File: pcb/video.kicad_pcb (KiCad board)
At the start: 4 copper layers, 159.9 x 99.9 mm, 174 parts, among them J1 09031966921, J3 Conn_01x06, J4 Conn_01x06, J5 Conn_01x06, J6 Conn_01x06, J7 DB15_Female_HighDensity, J8 HDMI_A, U1 NCP115, U10 NCA9306DPH, U2 LP3853ESX-3.3/NOPB, U3 LCMXO2-1200HC-4TG100I, U4 LCMXO2-7000HC-4TG144C, U5 THS8136, U6 TFP410PAP, U7 ESD224DQA, U8 ESD224DQA, U9 PCA9540BDP, X1 ASV-xxxMHz

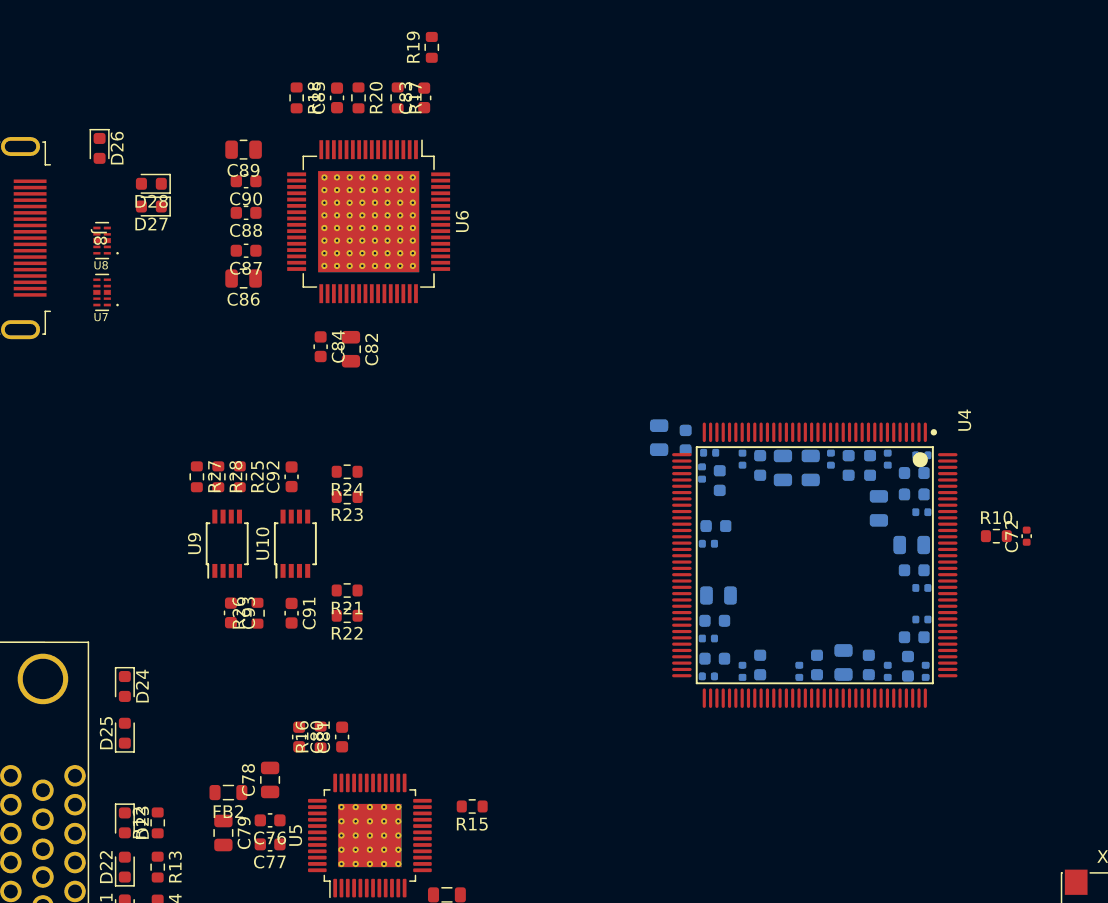
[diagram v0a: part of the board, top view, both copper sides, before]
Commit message: add traces for hdmi interface with proper anti crosstalk
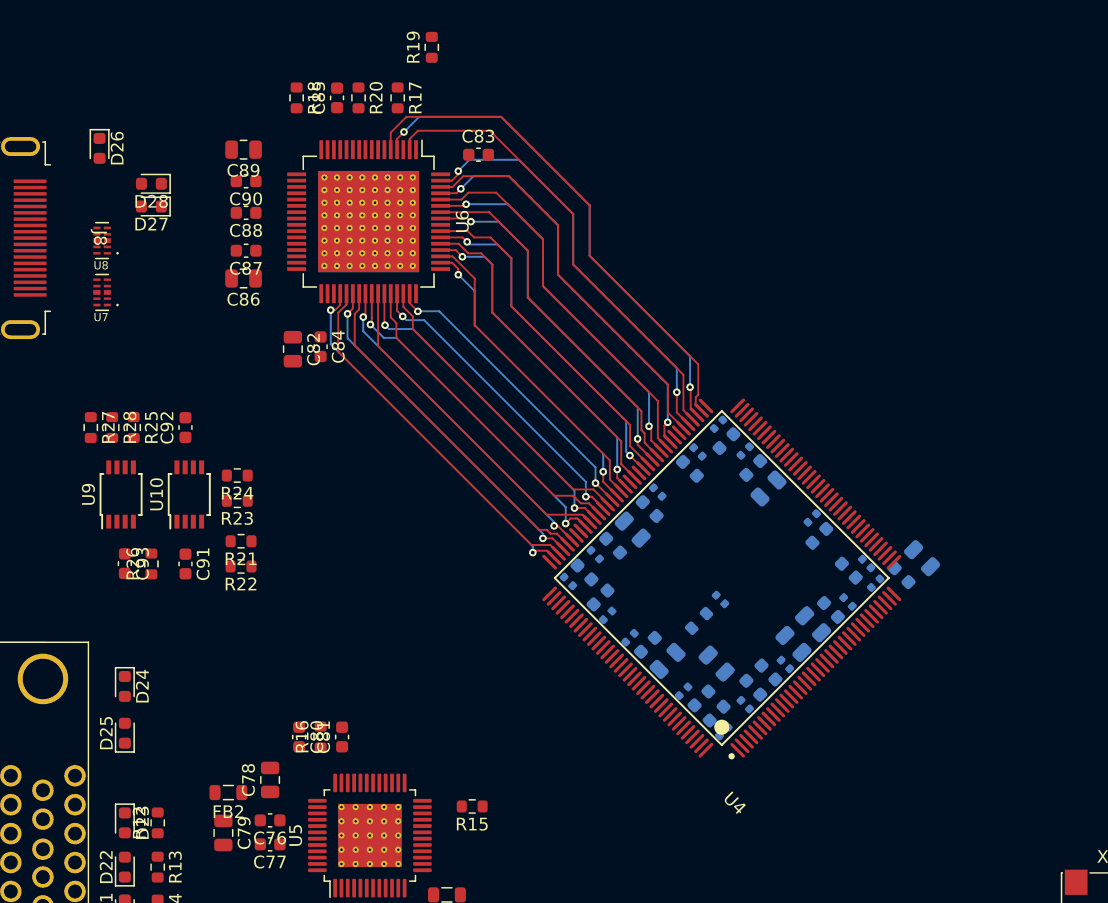
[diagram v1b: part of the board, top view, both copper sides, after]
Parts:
- C72, R10: moved to B.Cu
- moved C39 29.2 mm to (108.0, 96.3), turned to -45 degrees
- moved C38 26.9 mm to (120.3, 108.2), turned to 45 degrees
- moved C35 26.7 mm to (109.3, 95.6), turned to -45 degrees
- moved C47 25.0 mm to (110.5, 97.6), turned to 45 degrees
- moved C49 24.9 mm to (110.1, 94.2), turned to -45 degrees
- moved C42 24.9 mm to (111.1, 99.0), turned to 45 degrees
- moved C72 24.8 mm to (120.0, 97.7), turned to -45 degrees
- moved C36 24.6 mm to (119.7, 106.8), turned to 45 degrees
- moved R10 24.5 mm to (118.3, 99.4), turned to 45 degrees
- moved C44 23.6 mm to (117.1, 105.0), turned to 45 degrees
- moved C43 23.4 mm to (112.9, 100.8), turned to 45 degrees
- moved C46 23.3 mm to (118.5, 105.6), turned to 45 degrees
- moved C33 22.9 mm to (136.0, 94.5), turned to -45 degrees
- moved C71 22.5 mm to (122.0, 106.1), turned to 135 degrees
- moved C53 22.3 mm to (111.5, 93.5), turned to -45 degrees
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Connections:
- net /Video FPGA - Power/PLLIN renamed /Video FPGA/PLLIN
- net /Video FPGA - Power/TCK renamed /Video FPGA/TCK
- net /Video FPGA - Power/TDI renamed /Video FPGA/TDI
- net /Video FPGA - Power/TDO renamed /Video FPGA/TDO
- net /Video FPGA - Power/TMS renamed /Video FPGA/TMS
- D17 pad 2: /Video FPGA - Power/SN -> /Video FPGA/SN
- J6 pad 5: /Video FPGA - Power/SN -> /Video FPGA/SN
- R11 pad 2: /Video FPGA - Power/SN -> /Video FPGA/SN
- U4 pad 100: unconnected-(U4B-PR5A/(DQ0)) -> HDMI_D18
- U4 pad 103: unconnected-(U4B-PR4C) -> HDMI_D19
- U4 pad 104: unconnected-(U4B-PR3B/R_GPLLC_IN/(DQ0)) -> HDMI_D20
- U4 pad 105: unconnected-(U4B-PR3A/R_GPLLT_IN/(DQ0)) -> HDMI_D21
- U4 pad 106: unconnected-(U4B-PR2B/R_GPLLC_FB/(DQ0)) -> HDMI_D22
- U4 pad 107: unconnected-(U4B-PR2A/R_GPLLT_FB/(DQ0)) -> HDMI_D23
- U4 pad 70: /Video FPGA - Power/SN -> unconnected-(U4C-PB38A/SN)
- U4 pad 74: unconnected-(U4B-PR24A/(DQ1)) -> HDMI_VSYNC
- U4 pad 75: unconnected-(U4B-PR23B/(DQ1)) -> HDMI_HSYNC
- U4 pad 76: unconnected-(U4B-PR23A/(DQ1)) -> HDMI_DE
- U4 pad 77: unconnected-(U4B-PR21B/(DQ1)) -> HDMI_D0
- U4 pad 78: unconnected-(U4B-PR21A/(DQ1)) -> HDMI_D1
- U4 pad 81: unconnected-(U4B-PR18B/(DQ1)) -> HDMI_D2
- U4 pad 82: unconnected-(U4B-PR18A/(DQ1)) -> HDMI_D3
- U4 pad 83: unconnected-(U4B-PR17B/(DQ1)) -> HDMI_D4
- U4 pad 84: unconnected-(U4B-PR17A/(DQ1)) -> HDMI_D5
- U4 pad 85: unconnected-(U4B-PR16B/(DQS1N)) -> HDMI_CLK
- U4 pad 86: unconnected-(U4B-PR16A/(DQS1)) -> HDMI_D6
- U4 pad 87: unconnected-(U4B-PR15B) -> HDMI_D7
- U4 pad 89: unconnected-(U4B-PR15A) -> HDMI_D8
- U4 pad 91: unconnected-(U4B-PR12B/PCLKC1_0/(DQ0)) -> HDMI_D9
- U4 pad 92: unconnected-(U4B-PR12A/PCLKT1_0/(DQ0)) -> HDMI_D10
- U4 pad 93: unconnected-(U4B-PR11B/(DQS0N)) -> HDMI_D11
- U4 pad 94: unconnected-(U4B-PR11A/(DQS0)) -> HDMI_D12
- U4 pad 95: unconnected-(U4B-PR9B/(DQ0)) -> HDMI_D13
- U4 pad 96: unconnected-(U4B-PR9A/(DQ0)) -> HDMI_D14
- U4 pad 97: unconnected-(U4B-PR7B/(DQ0)) -> HDMI_D15
- U4 pad 98: unconnected-(U4B-PR7A/(DQ0)) -> HDMI_D16
- U4 pad 99: unconnected-(U4B-PR5B/(DQ0)) -> HDMI_D17
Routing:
- net HDMI_VSYNC: track 0.00 -> 40.6 mm
- net HDMI_HSYNC: track 0.00 -> 39.8 mm, vias 0 -> 2
- net HDMI_DE: track 0.00 -> 37.0 mm
- net HDMI_D0: track 0.00 -> 33.5 mm, vias 0 -> 2
- net HDMI_D2: track 0.00 -> 32.5 mm, vias 0 -> 2
- net HDMI_D1: track 0.00 -> 31.4 mm
- net HDMI_D3: track 0.00 -> 30.3 mm
- net HDMI_D4: track 0.00 -> 29.9 mm, vias 0 -> 2
- net HDMI_D23: track 0.00 -> 29.6 mm, vias 0 -> 2
- net HDMI_D22: track 0.00 -> 28.9 mm
- net HDMI_D5: track 0.00 -> 28.6 mm
- net HDMI_CLK: track 0.00 -> 28.6 mm, vias 0 -> 2
- net HDMI_D21: track 0.00 -> 27.9 mm, vias 0 -> 2
- net HDMI_D20: track 0.00 -> 27.6 mm
- net HDMI_D7: track 0.00 -> 27.3 mm, vias 0 -> 2
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
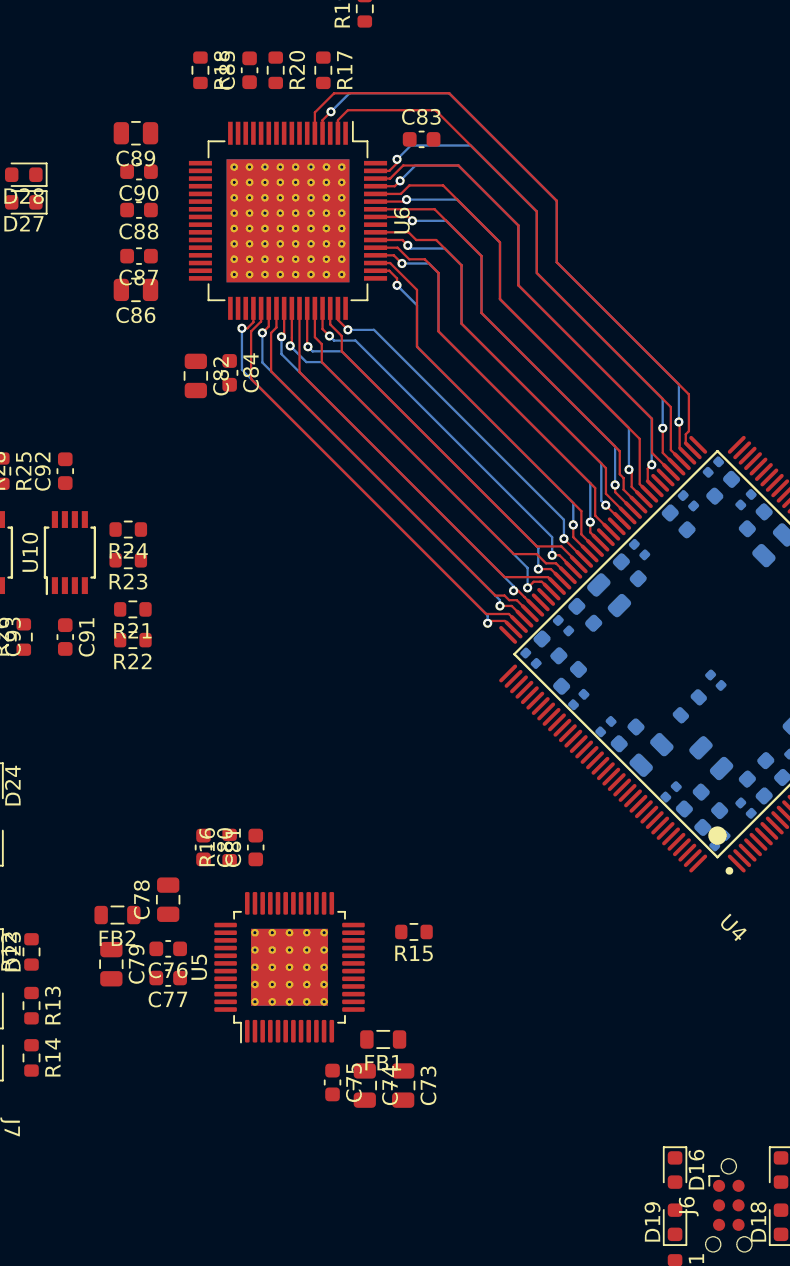
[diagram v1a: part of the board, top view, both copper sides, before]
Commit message: add via stitching near hdmi parallel bus vias
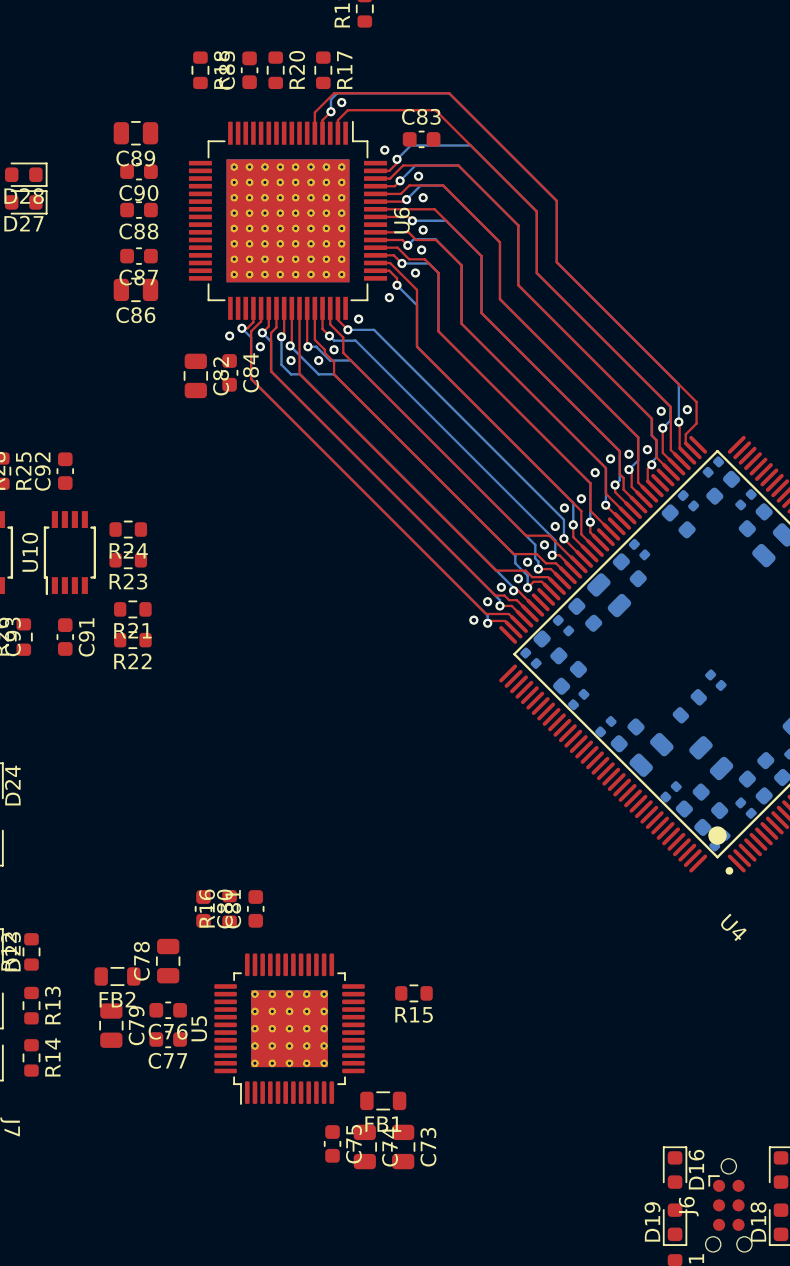
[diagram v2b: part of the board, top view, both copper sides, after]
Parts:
- moved C73 4.00 mm to (99.7, 128.1)
- moved C74 4.00 mm to (97.2, 128.1)
- moved C75 4.00 mm to (95.1, 127.9)
- moved C76 4.00 mm to (84.4, 119.2)
- moved C77 4.00 mm to (84.4, 121.1)
- moved C78 4.00 mm to (84.4, 116.0)
- moved C79 4.00 mm to (80.7, 120.2)
- moved C80 4.00 mm to (86.7, 112.6)
- moved C81 4.00 mm to (90.1, 112.6)
- moved FB1 4.00 mm to (98.4, 125.1)
- moved FB2 4.00 mm to (81.1, 117.0)
- moved R15 4.00 mm to (100.4, 118.1)
- moved R16 4.00 mm to (88.4, 112.6)
- moved U5 4.00 mm to (92.3, 120.4)
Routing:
- net HDMI_D4: track 29.9 -> 31.2 mm
- net GND: vias 0 -> 29
- added copper zone on In1.Cu, net GND
